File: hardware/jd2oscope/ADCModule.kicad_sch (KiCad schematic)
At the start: 16 parts, among them J2 CONBNC001, U4 OPA192IDBVR, U5 ADS7279IPW

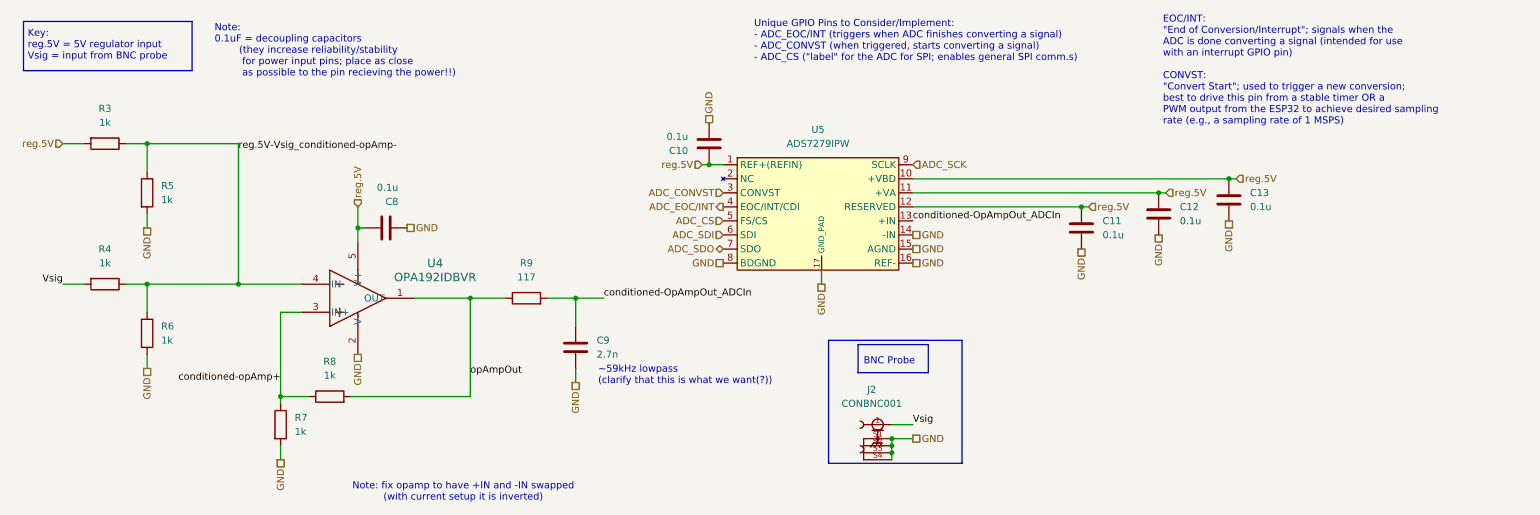
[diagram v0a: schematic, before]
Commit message: feat: updated capacitor values
and other fixes too
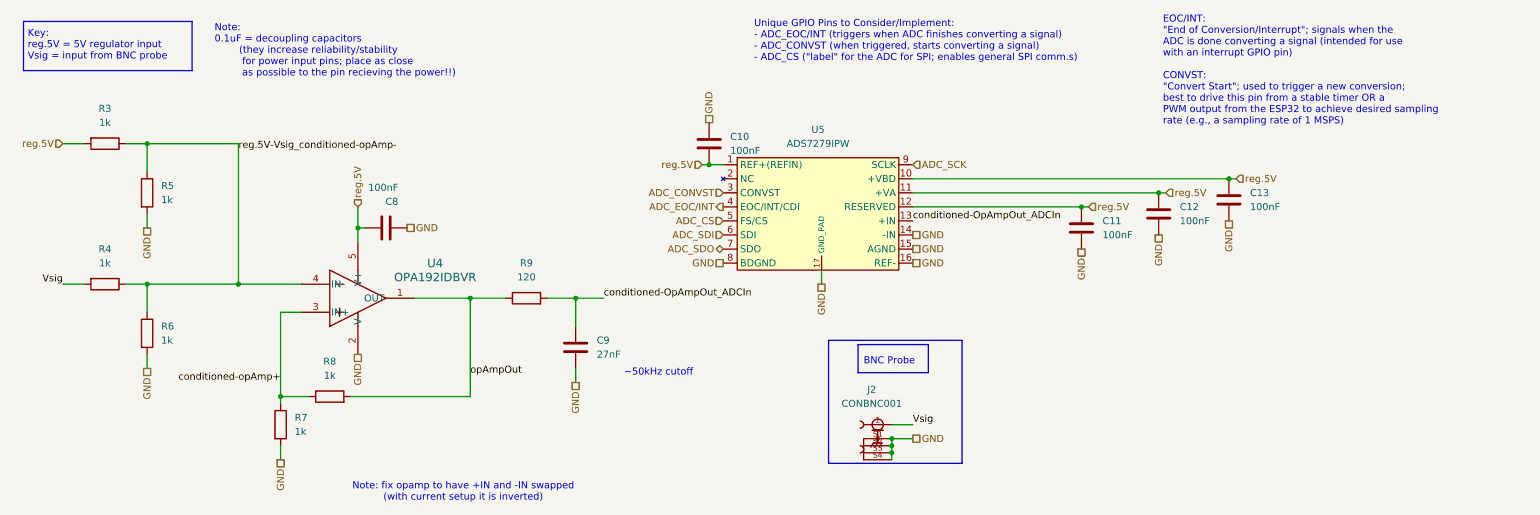
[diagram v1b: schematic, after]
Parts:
- C10, C11, C12, C13, C8: value 0.1u -> 100nF
- C9: value 2.7n -> 27nF
- R9: value 117 -> 120
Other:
- note added: "~50kHz cutoff"
- note removed: "~59kHz lowpass (clarify that this is what we want(?))"
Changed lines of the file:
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@@
 		)
 	)
-	(text "~59kHz lowpass\n(clarify that this is what we want(?))"
+	(text "~50kHz cutoff"
 		(exclude_from_sim no)
-		(at 119.634 80.01 0)
-		(effects
-			(font
-				(size 1.27 1.27)
-			)
-			(justify left)
+		(at 130.556 79.502 0)
+		(effects
+			(font
+				(size 1.27 1.27)
+			)
 		)
 	)
@@
 		(fields_autoplaced yes)
 		(property "Reference" "C10"
-			(at 135.89 39.3701 0)
-			(effects
-				(font
-					(size 1.27 1.27)
-				)
-				(justify left)
-			)
-		)
-		(property "Value" "0.1u"
-			(at 135.89 36.8301 0)
-			(effects
-				(font
-					(size 1.27 1.27)
-				)
-				(justify left)
+			(at 143.51 36.8299 0)
+			(effects
+				(font
+					(size 1.27 1.27)
+				)
+				(justify right)
+			)
+		)
+		(property "Value" "100nF"
+			(at 143.51 39.3699 0)
+			(effects
+				(font
+					(size 1.27 1.27)
+				)
+				(justify right)
 			)
 		)
@@
 			)
 		)
-		(property "Value" "2.7n"
+		(property "Value" "27nF"
 			(at 119.38 76.1999 0)
 			(effects
@@
 			)
 		)
-		(property "Value" "0.1u"
+		(property "Value" "100nF"
 			(at 210.82 54.6099 0)
 			(effects
@@
 			)
 		)
-		(property "Value" "0.1u"
+		(property "Value" "100nF"
 			(at 83.5025 46.0376 90)
 			(effects
@@
 			)
 		)
-		(property "Value" "117"
+		(property "Value" "120"
 			(at 106.68 62.23 90)
 			(effects
@@
 			)
 		)
-		(property "Value" "0.1u"
+		(property "Value" "100nF"
 			(at 224.79 52.0699 0)
 			(effects
@@
 			)
 		)
-		(property "Value" "0.1u"
+		(property "Value" "100nF"
 			(at 237.49 49.5299 0)
 			(effects
